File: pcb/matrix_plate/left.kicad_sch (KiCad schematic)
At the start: 31 parts

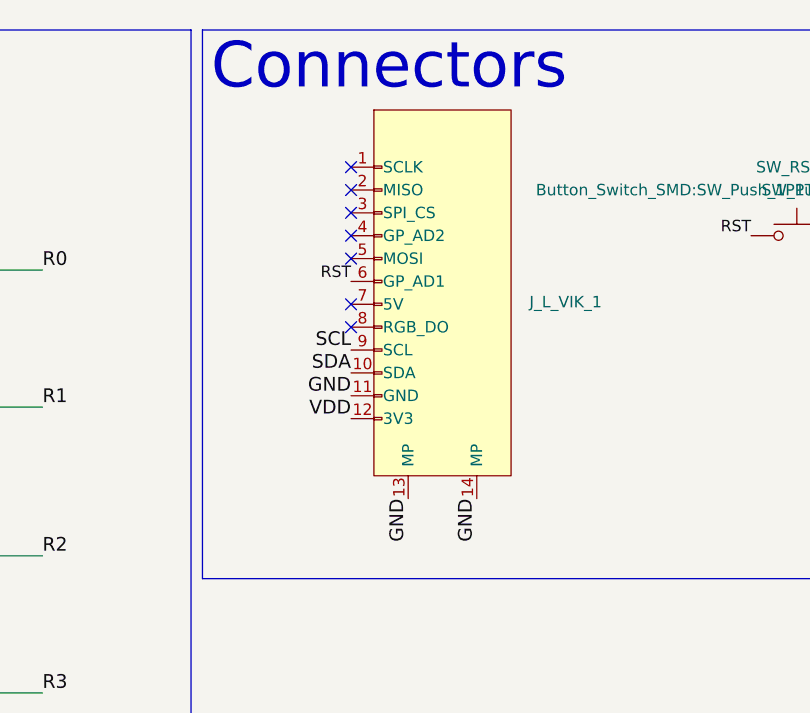
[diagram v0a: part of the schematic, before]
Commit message: Update KiCAD projects to use new library locations.
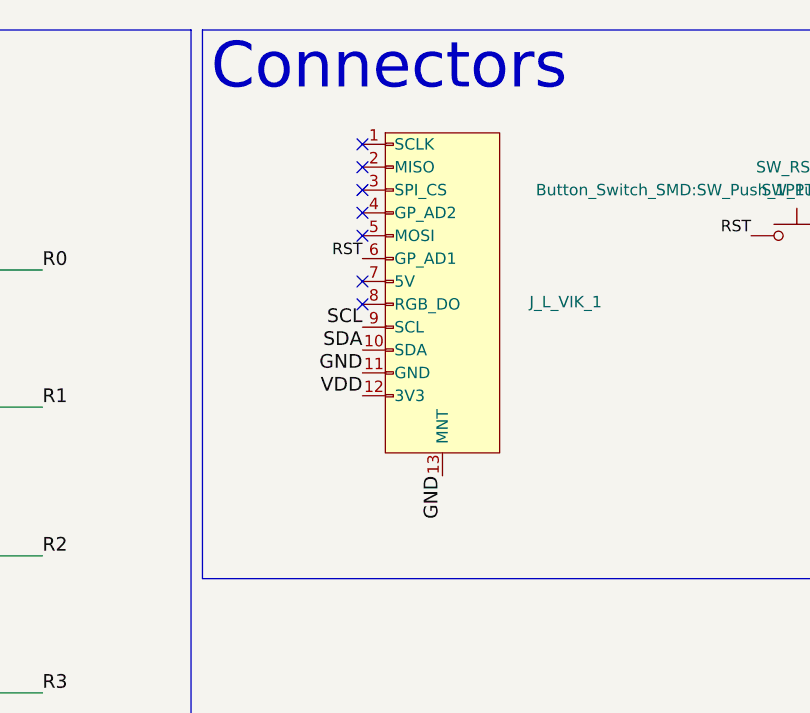
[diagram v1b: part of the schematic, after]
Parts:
- J_L_VIK_1: footprint vik:vik-module-connector-horizontal -> footprints:vik-module-connector-horizontal
- S_L_00, S_L_01, S_L_02, S_L_03, S_L_04, S_L_10, S_L_11, S_L_12, S_L_13, S_L_14, S_L_15, S_L_20, S_L_21, S_L_22, S_L_23, S_L_24, S_L_25, S_L_31, S_L_32, S_L_33, S_L_34, S_L_35: footprint key-switches:SW_GLP_Kailh_Choc_V1V2_HotSwap_PTH -> footprints:SW_GLP_Kailh_Choc_V1V2_HotSwap_PTH
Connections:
- net GND: no longer J_L_VIK_1.14 (MP)
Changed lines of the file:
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@@
 	)
 	(no_connect
-		(at 293.37 30.48)
+		(at 294.64 27.94)
 	)
 	(no_connect
-		(at 293.37 27.94)
+		(at 294.64 25.4)
 	)
 	(no_connect
-		(at 293.37 45.72)
+		(at 294.64 43.18)
 	)
 	(no_connect
@@
 	)
 	(no_connect
-		(at 293.37 33.02)
+		(at 294.64 30.48)
 	)
 	(no_connect
-		(at 293.37 35.56)
+		(at 294.64 33.02)
 	)
 	(no_connect
-		(at 293.37 38.1)
+		(at 294.64 35.56)
 	)
 	(no_connect
-		(at 293.37 43.18)
+		(at 294.64 40.64)
 	)
 	(no_connect
@@
 	)
 	(label "GND"
-		(at 293.37 53.34 180)
+		(at 294.64 50.8 180)
 		(effects
 			(font
@@
 	)
 	(label "GND"
-		(at 307.34 64.77 270)
-		(effects
-			(font
-				(size 1.524 1.524)
-			)
-			(justify right bottom)
-		)
-	)
-	(label "GND"
-		(at 299.72 64.77 270)
+		(at 303.53 62.23 270)
 		(effects
 			(font
@@
 	)
 	(label "VDD"
-		(at 293.37 55.88 180)
+		(at 294.64 53.34 180)
 		(effects
 			(font
@@
 	)
 	(label "SCL"
-		(at 293.37 48.26 180)
+		(at 294.64 45.72 180)
 		(effects
 			(font
@@
 	)
 	(label "RST"
-		(at 293.37 40.64 180)
+		(at 294.64 38.1 180)
 		(effects
 			(font
@@
 	)
 	(label "SDA"
-		(at 293.37 50.8 180)
+		(at 294.64 48.26 180)
 		(effects
 			(font
@@
 			)
 		)
-		(property "Footprint" "key-switches:SW_GLP_Kailh_Choc_V1V2_HotSwap_PTH"
+		(property "Footprint" "footprints:SW_GLP_Kailh_Choc_V1V2_HotSwap_PTH"
 			(at 227.33 68.58 0)
 			(hide yes)
@@
 			)
 		)
-		(property "Footprint" "key-switches:SW_GLP_Kailh_Choc_V1V2_HotSwap_PTH"
+		(property "Footprint" "footprints:SW_GLP_Kailh_Choc_V1V2_HotSwap_PTH"
 			(at 209.55 68.58 0)
 			(hide yes)
@@
 			)
 		)
-		(property "Footprint" "key-switches:SW_GLP_Kailh_Choc_V1V2_HotSwap_PTH"
+		(property "Footprint" "footprints:SW_GLP_Kailh_Choc_V1V2_HotSwap_PTH"
 			(at 245.11 52.07 0)
 			(hide yes)
@@
 			)
 		)
-		(property "Footprint" "key-switches:SW_GLP_Kailh_Choc_V1V2_HotSwap_PTH"
+		(property "Footprint" "footprints:SW_GLP_Kailh_Choc_V1V2_HotSwap_PTH"
 			(at 156.21 36.83 0)
 			(hide yes)
@@
 			)
 		)
-		(property "Footprint" "key-switches:SW_GLP_Kailh_Choc_V1V2_HotSwap_PTH"
+		(property "Footprint" "footprints:SW_GLP_Kailh_Choc_V1V2_HotSwap_PTH"
 			(at 209.55 36.83 0)
 			(hide yes)
@@
 			)
 		)
-		(property "Footprint" "key-switches:SW_GLP_Kailh_Choc_V1V2_HotSwap_PTH"
+		(property "Footprint" "footprints:SW_GLP_Kailh_Choc_V1V2_HotSwap_PTH"
 			(at 156.21 68.58 0)
 			(hide yes)
@@
 			)
 		)
-		(property "Footprint" "key-switches:SW_GLP_Kailh_Choc_V1V2_HotSwap_PTH"
+		(property "Footprint" "footprints:SW_GLP_Kailh_Choc_V1V2_HotSwap_PTH"
 			(at 227.33 83.82 0)
 			(hide yes)
@@
 			)
 		)
-		(property "Footprint" "key-switches:SW_GLP_Kailh_Choc_V1V2_HotSwap_PTH"
+		(property "Footprint" "footprints:SW_GLP_Kailh_Choc_V1V2_HotSwap_PTH"
 			(at 209.55 83.82 0)
 			(hide yes)
@@
 			)
 		)
-		(property "Footprint" "key-switches:SW_GLP_Kailh_Choc_V1V2_HotSwap_PTH"
+		(property "Footprint" "footprints:SW_GLP_Kailh_Choc_V1V2_HotSwap_PTH"
 			(at 227.33 52.07 0)
 			(hide yes)
@@
 			)
 		)
-		(property "Footprint" "key-switches:SW_GLP_Kailh_Choc_V1V2_HotSwap_PTH"
+		(property "Footprint" "footprints:SW_GLP_Kailh_Choc_V1V2_HotSwap_PTH"
 			(at 173.99 36.83 0)
 			(hide yes)
@@
 			)
 		)
-		(property "Footprint" "vik:vik-module-connector-horizontal"
-			(at 303.53 35.56 0)
+		(property "Footprint" "footprints:vik-module-connector-horizontal"
+			(at 302.26 31.75 0)
 			(hide yes)
 			(show_name no)
@@
 		)
 		(property "Datasheet" ""
-			(at 303.53 35.56 0)
+			(at 302.26 31.75 0)
 			(hide yes)
 			(show_name no)
@@
 		)
 		(property "Description" "VIK_IN_INTC"
-			(at 314.96 45.974 0)
+			(at 302.26 38.1 0)
 			(hide yes)
 			(show_name no)
@@
 		(pin "13"
 		)
-		(pin "14"
-		)
 		(instances
 			(project "matrix_plate"
@@
 			)
 		)
-		(property "Footprint" "key-switches:SW_GLP_Kailh_Choc_V1V2_HotSwap_PTH"
+		(property "Footprint" "footprints:SW_GLP_Kailh_Choc_V1V2_HotSwap_PTH"
 			(at 191.77 68.58 0)
 			(hide yes)
@@
 			)
 		)
-		(property "Footprint" "key-switches:SW_GLP_Kailh_Choc_V1V2_HotSwap_PTH"
+		(property "Footprint" "footprints:SW_GLP_Kailh_Choc_V1V2_HotSwap_PTH"
 			(at 173.99 52.07 0)
 			(hide yes)
@@
 			)
 		)
-		(property "Footprint" "key-switches:SW_GLP_Kailh_Choc_V1V2_HotSwap_PTH"
+		(property "Footprint" "footprints:SW_GLP_Kailh_Choc_V1V2_HotSwap_PTH"
 			(at 191.77 36.83 0)
 			(hide yes)
@@
 			)
 		)
-		(property "Footprint" "key-switches:SW_GLP_Kailh_Choc_V1V2_HotSwap_PTH"
+		(property "Footprint" "footprints:SW_GLP_Kailh_Choc_V1V2_HotSwap_PTH"
 			(at 173.99 68.58 0)
 			(hide yes)
@@
 			)
 		)
-		(property "Footprint" "key-switches:SW_GLP_Kailh_Choc_V1V2_HotSwap_PTH"
+		(property "Footprint" "footprints:SW_GLP_Kailh_Choc_V1V2_HotSwap_PTH"
 			(at 191.77 83.82 0)
 			(hide yes)
@@
 			)
 		)
-		(property "Footprint" "key-switches:SW_GLP_Kailh_Choc_V1V2_HotSwap_PTH"
+		(property "Footprint" "footprints:SW_GLP_Kailh_Choc_V1V2_HotSwap_PTH"
 			(at 156.21 52.07 0)
 			(hide yes)
@@
 			)
 		)
-		(property "Footprint" "key-switches:SW_GLP_Kailh_Choc_V1V2_HotSwap_PTH"
+		(property "Footprint" "footprints:SW_GLP_Kailh_Choc_V1V2_HotSwap_PTH"
 			(at 245.11 68.58 0)
 			(hide yes)
@@
 			)
 		)
-		(property "Footprint" "key-switches:SW_GLP_Kailh_Choc_V1V2_HotSwap_PTH"
+		(property "Footprint" "footprints:SW_GLP_Kailh_Choc_V1V2_HotSwap_PTH"
 			(at 191.77 52.07 0)
 			(hide yes)
@@
 			)
 		)
-		(property "Footprint" "key-switches:SW_GLP_Kailh_Choc_V1V2_HotSwap_PTH"
+		(property "Footprint" "footprints:SW_GLP_Kailh_Choc_V1V2_HotSwap_PTH"
 			(at 227.33 36.83 0)
 			(hide yes)
@@
 			)
 		)
-		(property "Footprint" "key-switches:SW_GLP_Kailh_Choc_V1V2_HotSwap_PTH"
+		(property "Footprint" "footprints:SW_GLP_Kailh_Choc_V1V2_HotSwap_PTH"
 			(at 173.99 83.82 0)
 			(hide yes)
@@
 			)
 		)
-		(property "Footprint" "key-switches:SW_GLP_Kailh_Choc_V1V2_HotSwap_PTH"
+		(property "Footprint" "footprints:SW_GLP_Kailh_Choc_V1V2_HotSwap_PTH"
 			(at 245.11 83.82 0)
 			(hide yes)
@@
 			)
 		)
-		(property "Footprint" "key-switches:SW_GLP_Kailh_Choc_V1V2_HotSwap_PTH"
+		(property "Footprint" "footprints:SW_GLP_Kailh_Choc_V1V2_HotSwap_PTH"
 			(at 209.55 52.07 0)
 			(hide yes)
